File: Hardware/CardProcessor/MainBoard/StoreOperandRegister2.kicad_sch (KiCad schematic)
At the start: 2 parts, among them U43 74ABT16374

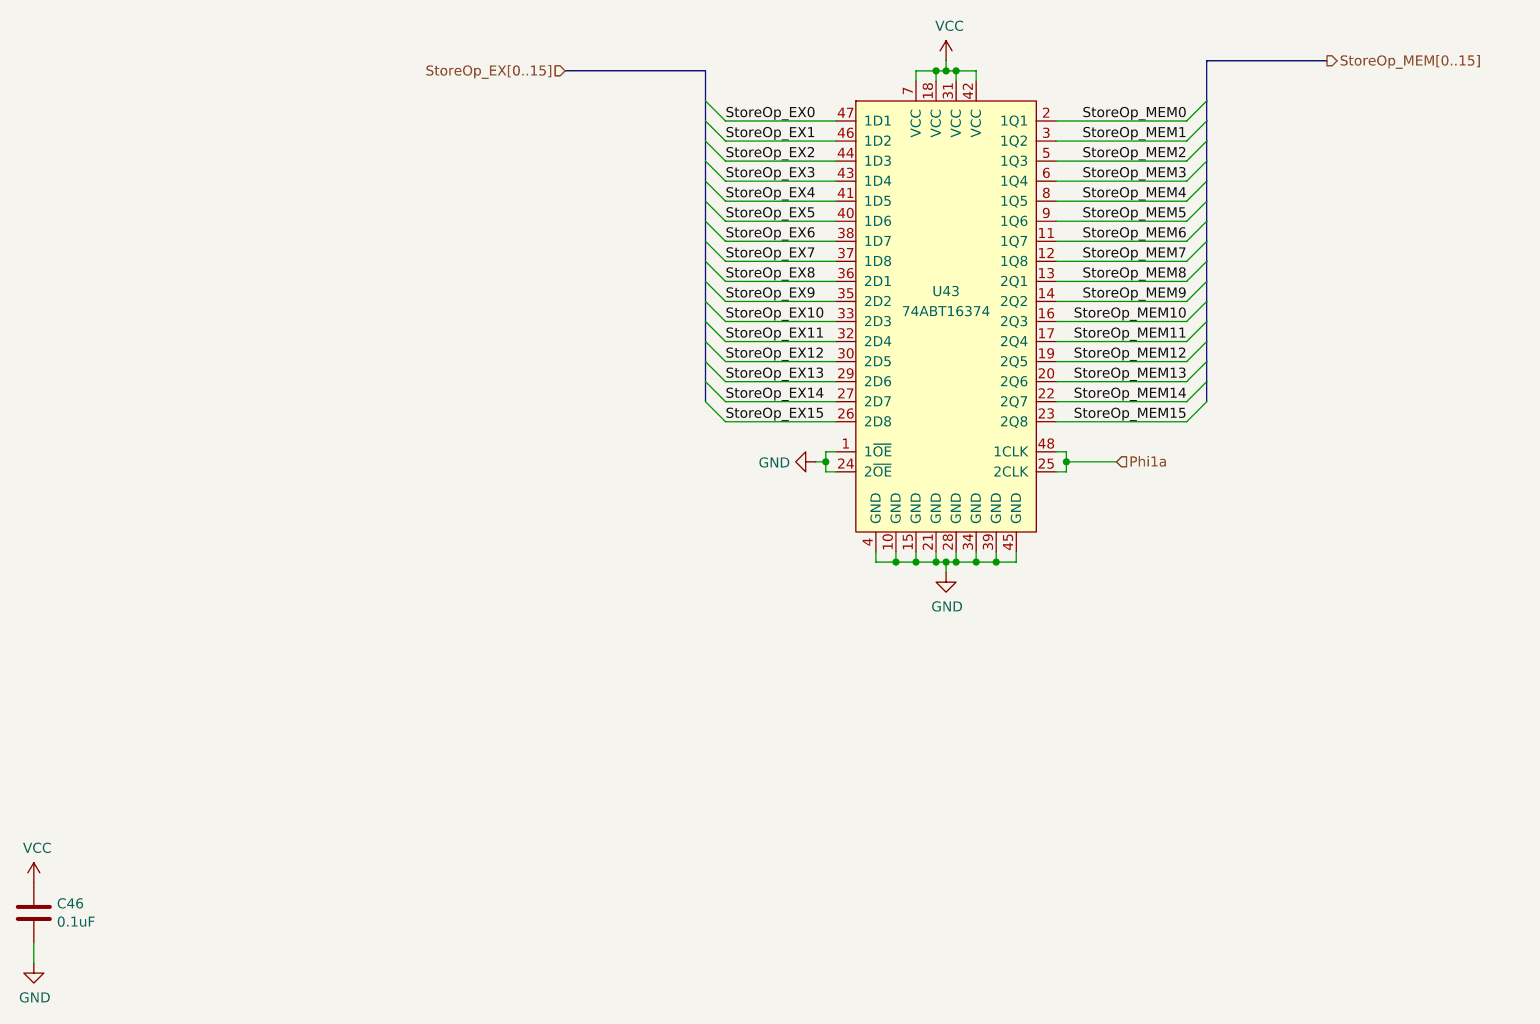
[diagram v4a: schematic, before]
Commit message: Automatically reannotate project and fix a few silkscreen-related issues
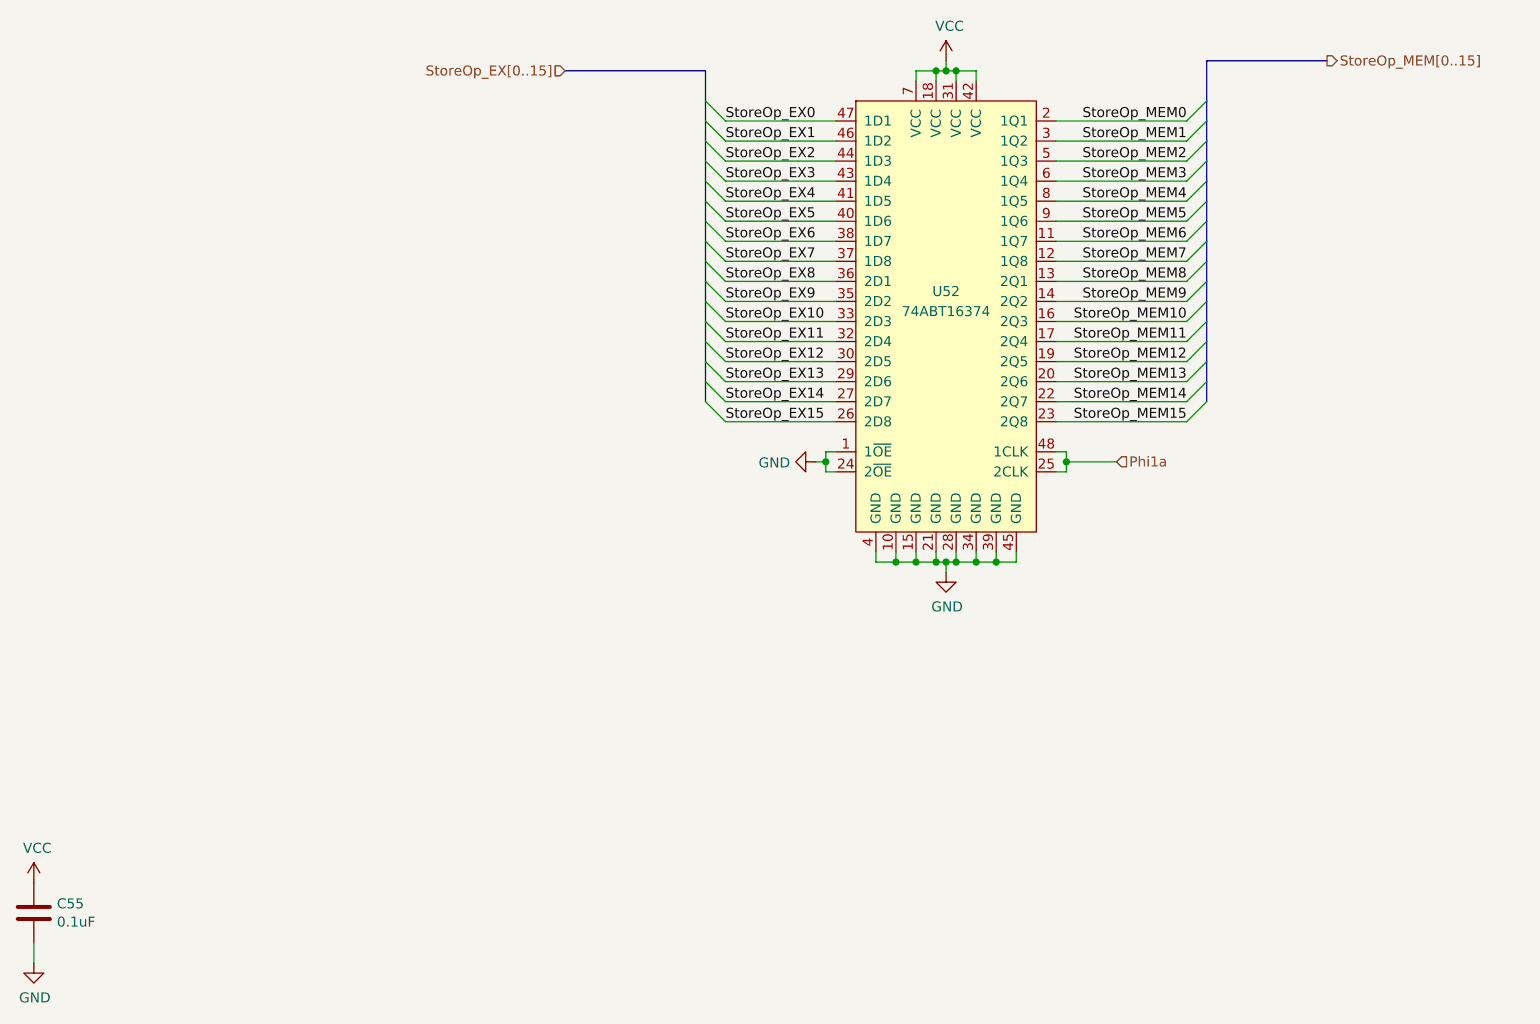
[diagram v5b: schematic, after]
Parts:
- renumbered C46 to C55, U43 to U52
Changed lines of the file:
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@@
 		(on_board yes)
 		(dnp no)
-		(property "Reference" "C46"
+		(property "Reference" "C55"
 			(at 32.131 177.9016 0)
 			(effects
@@
 			(project "MainBoard"
 				(path "/83c5181e-f5ee-453c-ae5c-d7256ba8837d/637456a4-4ee5-48ca-bb06-9734ef3462ed/54d68a2e-0685-421b-bbc3-ead3c7c2b0a7/00000000-0000-0000-0000-00005fd8d6fe"
-					(reference "C46")
+					(reference "C55")
 					(unit 1)
 				)
@@
 		(on_board yes)
 		(dnp no)
-		(property "Reference" "#PWR0110"
+		(property "Reference" "#PWR0336"
 			(at 29.21 179.07 0)
 			(effects
@@
 			(project "MainBoard"
 				(path "/83c5181e-f5ee-453c-ae5c-d7256ba8837d/637456a4-4ee5-48ca-bb06-9734ef3462ed/54d68a2e-0685-421b-bbc3-ead3c7c2b0a7/00000000-0000-0000-0000-00005fd8d6fe"
-					(reference "#PWR0110")
+					(reference "#PWR0336")
 					(unit 1)
 				)
@@
 		(on_board yes)
 		(dnp no)
-		(property "Reference" "#PWR0111"
+		(property "Reference" "#PWR0337"
 			(at 29.21 191.77 0)
 			(effects
@@
 			(project "MainBoard"
 				(path "/83c5181e-f5ee-453c-ae5c-d7256ba8837d/637456a4-4ee5-48ca-bb06-9734ef3462ed/54d68a2e-0685-421b-bbc3-ead3c7c2b0a7/00000000-0000-0000-0000-00005fd8d6fe"
-					(reference "#PWR0111")
+					(reference "#PWR0337")
 					(unit 1)
 				)
@@
 		(on_board yes)
 		(dnp no)
-		(property "Reference" "#PWR0112"
+		(property "Reference" "#PWR0338"
 			(at 121.92 121.92 0)
 			(effects
@@
 			(project "MainBoard"
 				(path "/83c5181e-f5ee-453c-ae5c-d7256ba8837d/637456a4-4ee5-48ca-bb06-9734ef3462ed/54d68a2e-0685-421b-bbc3-ead3c7c2b0a7/00000000-0000-0000-0000-00005fd8d6fe"
-					(reference "#PWR0112")
+					(reference "#PWR0338")
 					(unit 1)
 				)
@@
 		(on_board yes)
 		(dnp no)
-		(property "Reference" "#PWR0113"
+		(property "Reference" "#PWR0339"
 			(at 144.78 74.93 0)
 			(effects
@@
 			(project "MainBoard"
 				(path "/83c5181e-f5ee-453c-ae5c-d7256ba8837d/637456a4-4ee5-48ca-bb06-9734ef3462ed/54d68a2e-0685-421b-bbc3-ead3c7c2b0a7/00000000-0000-0000-0000-00005fd8d6fe"
-					(reference "#PWR0113")
+					(reference "#PWR0339")
 					(unit 1)
 				)
@@
 		(on_board yes)
 		(dnp no)
-		(property "Reference" "#PWR0114"
+		(property "Reference" "#PWR0340"
 			(at 144.78 142.24 0)
 			(effects
@@
 			(project "MainBoard"
 				(path "/83c5181e-f5ee-453c-ae5c-d7256ba8837d/637456a4-4ee5-48ca-bb06-9734ef3462ed/54d68a2e-0685-421b-bbc3-ead3c7c2b0a7/00000000-0000-0000-0000-00005fd8d6fe"
-					(reference "#PWR0114")
+					(reference "#PWR0340")
 					(unit 1)
 				)
@@
 		(on_board yes)
 		(dnp no)
-		(property "Reference" "U43"
+		(property "Reference" "U52"
 			(at 144.78 100.33 0)
 			(effects
@@
 			(project "MainBoard"
 				(path "/83c5181e-f5ee-453c-ae5c-d7256ba8837d/637456a4-4ee5-48ca-bb06-9734ef3462ed/54d68a2e-0685-421b-bbc3-ead3c7c2b0a7/00000000-0000-0000-0000-00005fd8d6fe"
-					(reference "U43")
-					(unit 1)
-				)
+					(reference "U52")
+					(unit 1)
+				)

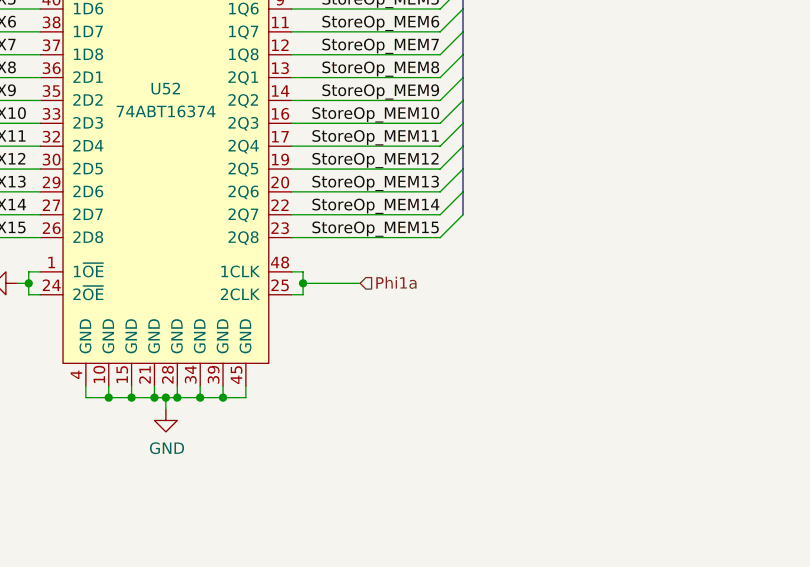
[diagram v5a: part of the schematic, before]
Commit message: Split net Phi1a into Phi1a and Phi1e
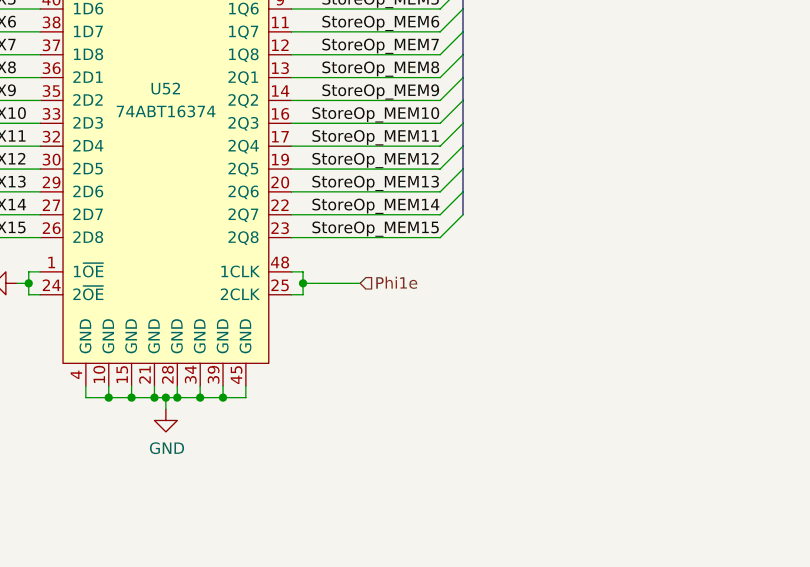
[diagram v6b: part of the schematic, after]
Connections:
- net Phi1a renamed Phi1e
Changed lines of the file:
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@@
 		)
 	)
-	(hierarchical_label "Phi1a"
+	(hierarchical_label "Phi1e"
 		(shape input)
 		(at 166.37 121.92 0)
